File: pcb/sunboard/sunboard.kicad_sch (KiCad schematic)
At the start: 3 parts, among them U1 CD74HC4067M, U2 CD74HC4067M, U3 ESP32-DEVKIT-V1

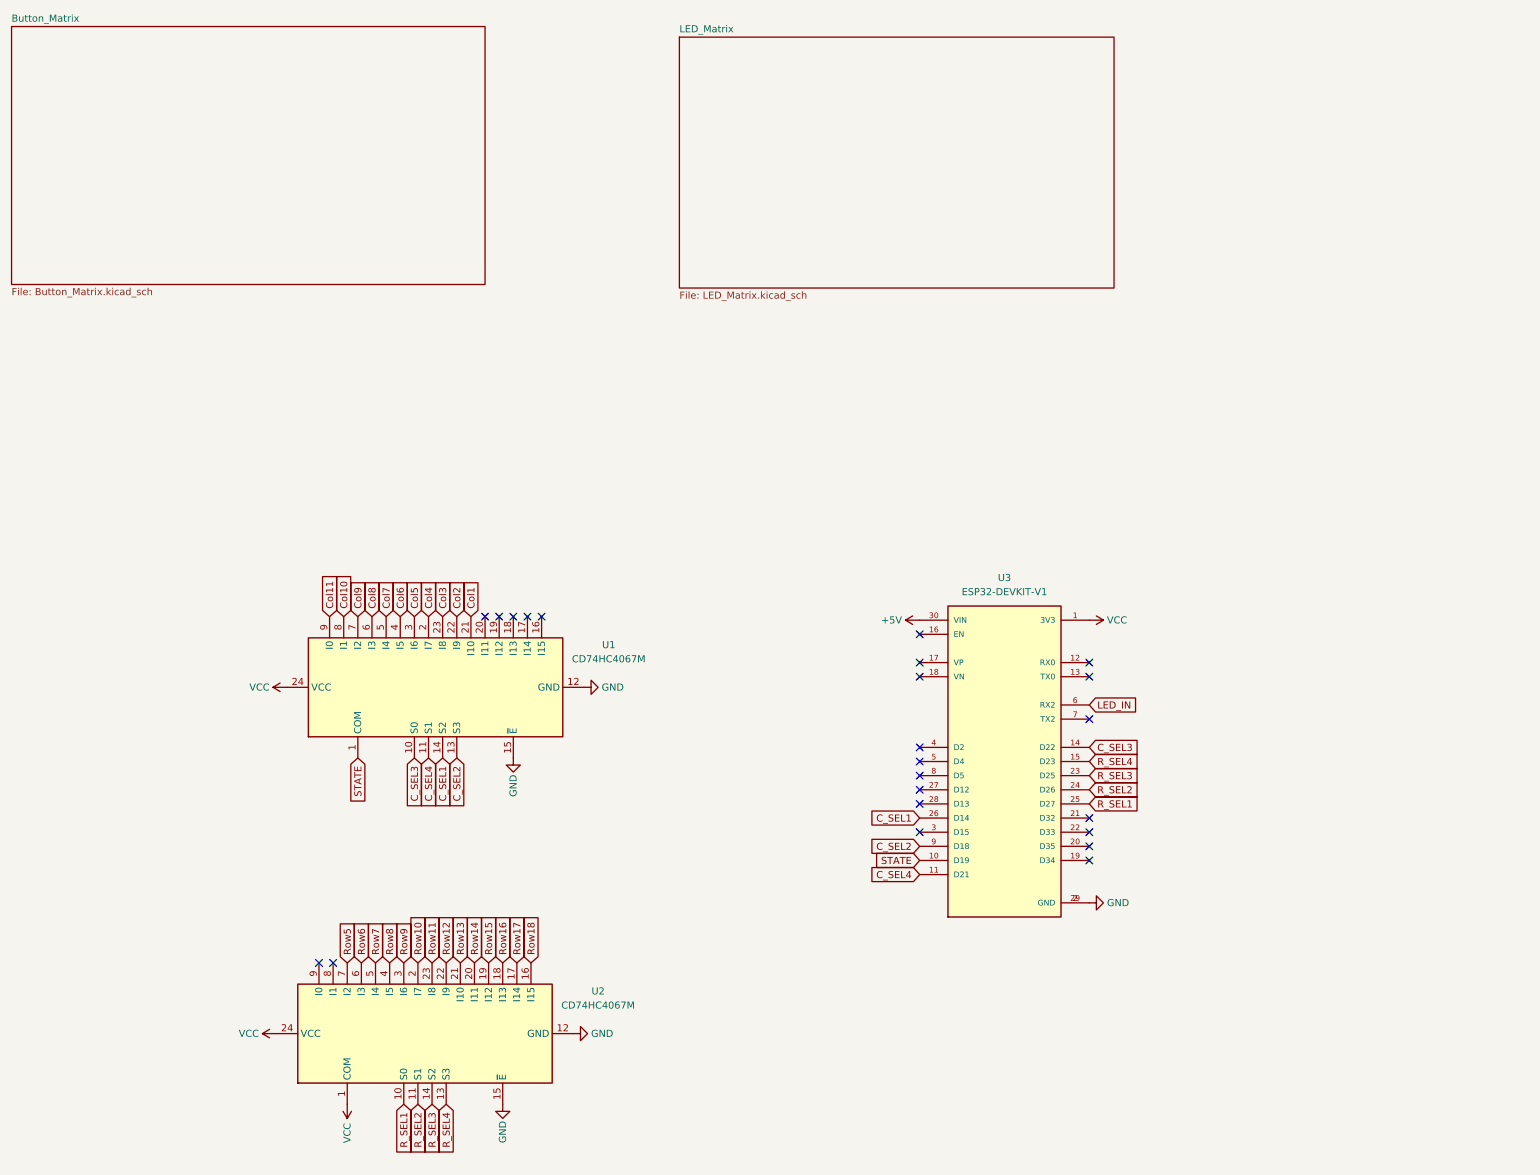
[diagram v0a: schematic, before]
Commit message: feat(pcb): add display
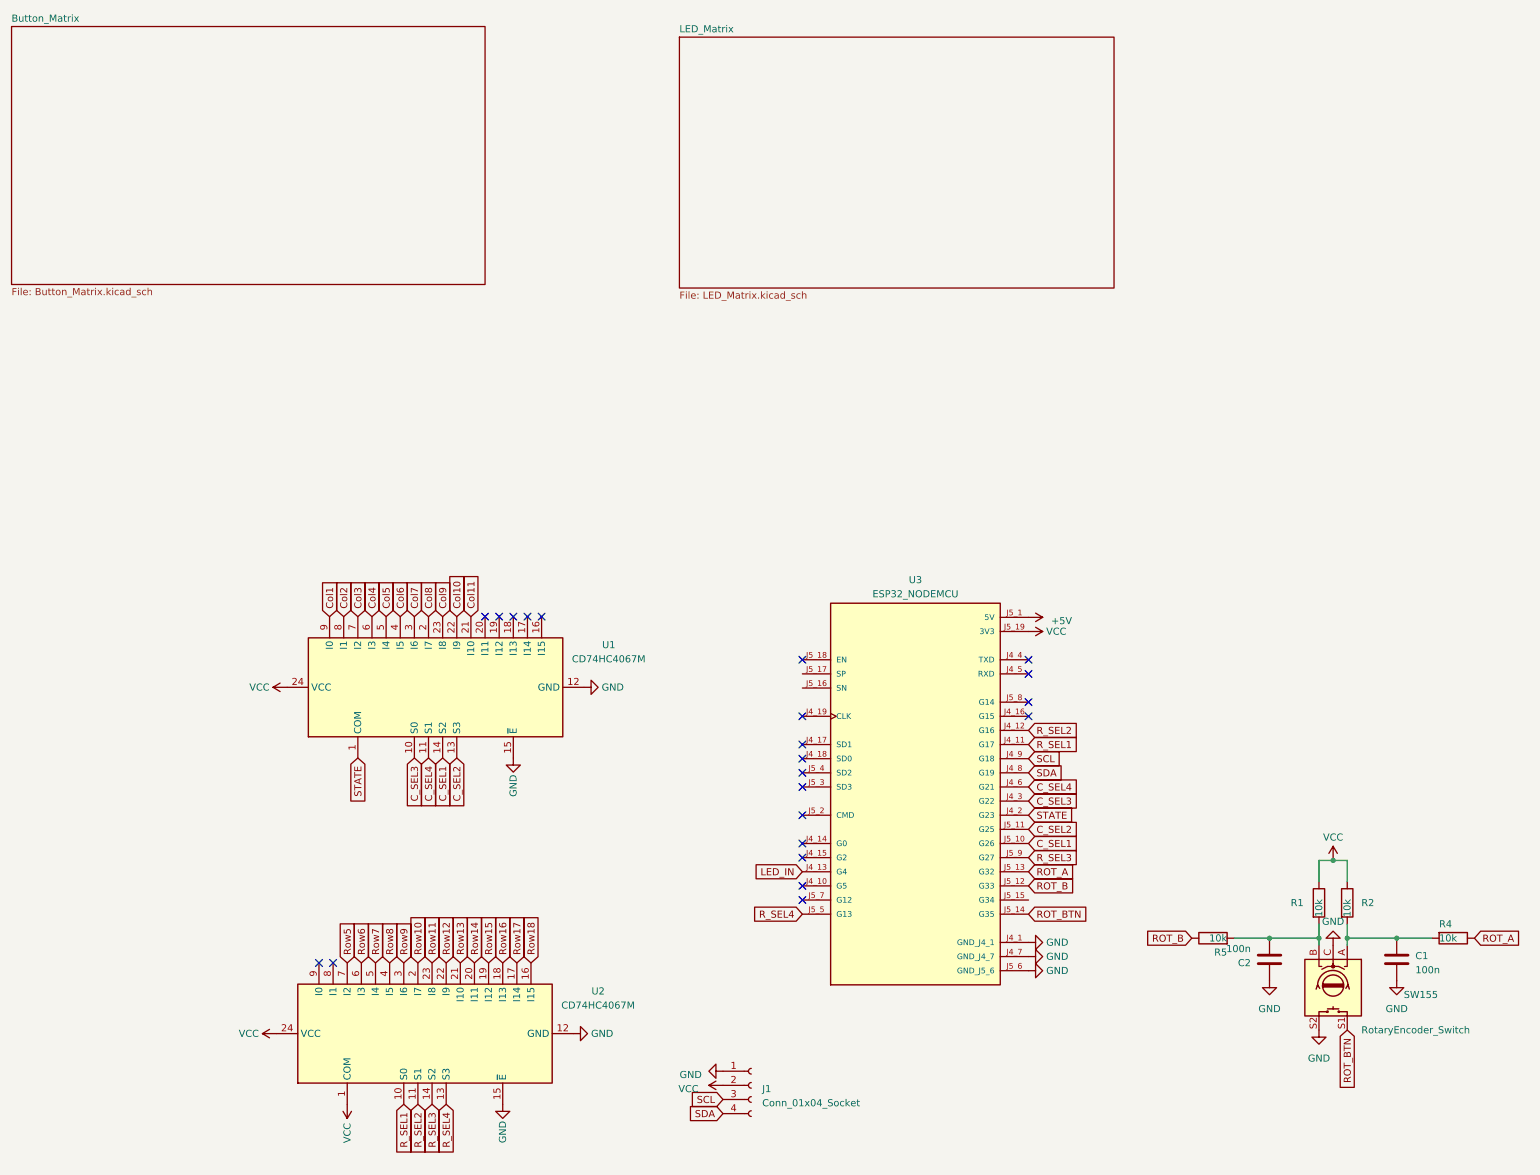
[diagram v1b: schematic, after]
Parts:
- removed U3: ESP32-DEVKIT-V1, ESP32-DEVKIT-V1:MODULE_ESP32_DEVKIT_V1, symbol ESP32-DEVKIT-V1:ESP32-DEVKIT-V1
- added C1, C2: 100n, Capacitor_SMD:C_0805_2012Metric, symbol Device:C
- added J1: Conn_01x04_Socket, Connector_PinSocket_2.54mm:PinSocket_1x04_P2.54mm_Vertical, symbol Connector:Conn_01x04_Socket
- added R1, R2, R4, R5: 10k, Resistor_SMD:R_0805_2012Metric, symbol Device:R
- added SW155: RotaryEncoder_Switch, Rotary_Encoder:RotaryEncoder_Alps_EC12E-Switch_Vertical_H20mm, symbol Device:RotaryEncoder_Switch
- added U3: ESP32_NODEMCU, ESP32_NODEMCU:MODULE_ESP32_NODEMCU, symbol ESP32_NODEMCU:ESP32_NODEMCU
- U1, U2: JLCPCB Part # (none) -> C496123
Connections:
- net +5V: now also U3.J5_1 (5V)
- net C_SEL1: now also U3.J5_10 (G26)
- net C_SEL2: now also U3.J5_11 (G25)
- net C_SEL3: now also U3.J4_3 (G22)
- net C_SEL4: now also U3.J4_6 (G21)
- net Col1: now also U1.9 (I0); no longer U1.21 (I10)
- net Col10: now also U1.22 (I9); no longer U1.8 (I1)
- net Col11: now also U1.21 (I10); no longer U1.9 (I0)
- net Col2: now also U1.8 (I1); no longer U1.22 (I9)
- net Col3: now also U1.7 (I2); no longer U1.23 (I8)
- net Col4: now also U1.6 (I3); no longer U1.2 (I7)
- net Col5: now also U1.5 (I4); no longer U1.3 (I6)
- net Col7: now also U1.3 (I6); no longer U1.5 (I4)
- net Col8: now also U1.2 (I7); no longer U1.6 (I3)
- net Col9: now also U1.23 (I8); no longer U1.7 (I2)
- net GND: now also C1.2, C2.1, J1.1 (Pin_1), SW155.C, SW155.S2, U3.J4_1 (GND_J4_1), U3.J4_7 (GND_J4_7), U3.J5_6 (GND_J5_6)
- net LED_IN: now also U3.J4_13 (G4)
- net R_SEL1: now also U3.J4_11 (G17)
- net R_SEL2: now also U3.J4_12 (G16)
- net R_SEL3: now also U3.J5_9 (G27)
- net R_SEL4: now also U3.J5_5 (G13)
- net STATE: now also U3.J4_2 (G23)
- net VCC: now also J1.2 (Pin_2), R1.1, R2.1, U3.J5_19 (3V3)
- new net: C1.1, R2.2, R4.2, SW155.A
- new net: C2.2, R1.2, R5.2, SW155.B
- new net ROT_A: R4.1, U3.J5_13 (G32)
- new net ROT_B: R5.1, U3.J5_12 (G33)
- new net ROT_BTN: SW155.S1, U3.J5_14 (G35)
- new net SCL: J1.3 (Pin_3), U3.J4_9 (G18)
- new net SDA: J1.4 (Pin_4), U3.J4_8 (G19)
- no-connect marks 23 -> 22

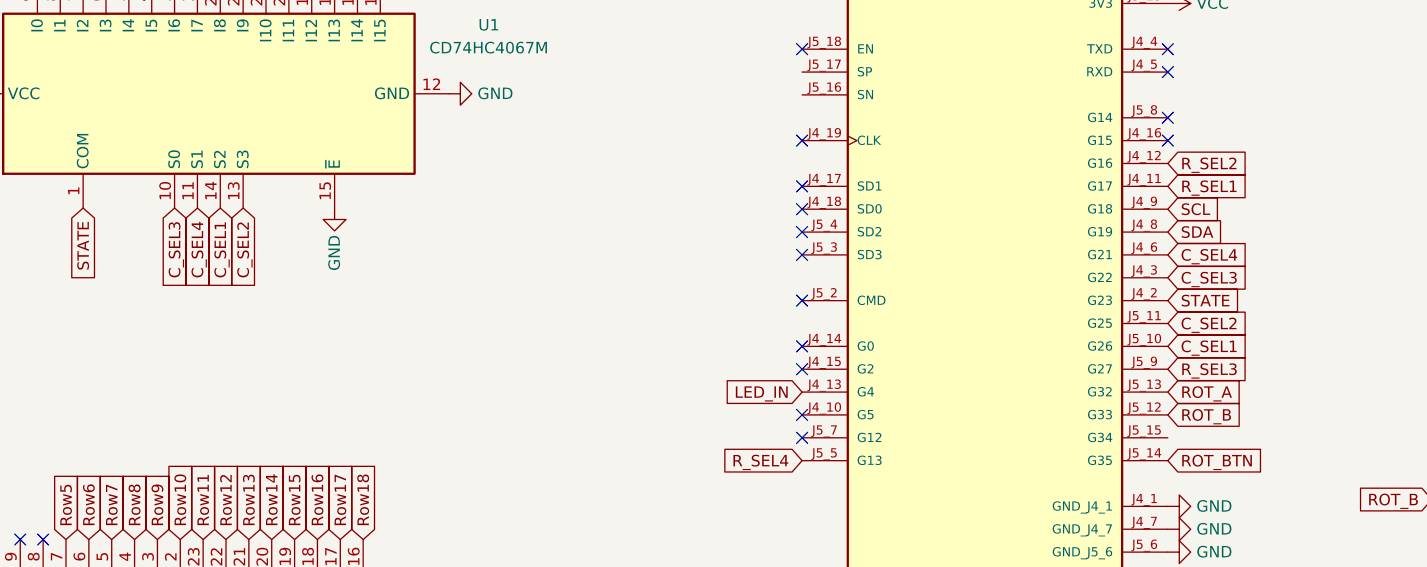
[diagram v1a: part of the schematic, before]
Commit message: feat(pcb): rename some labels
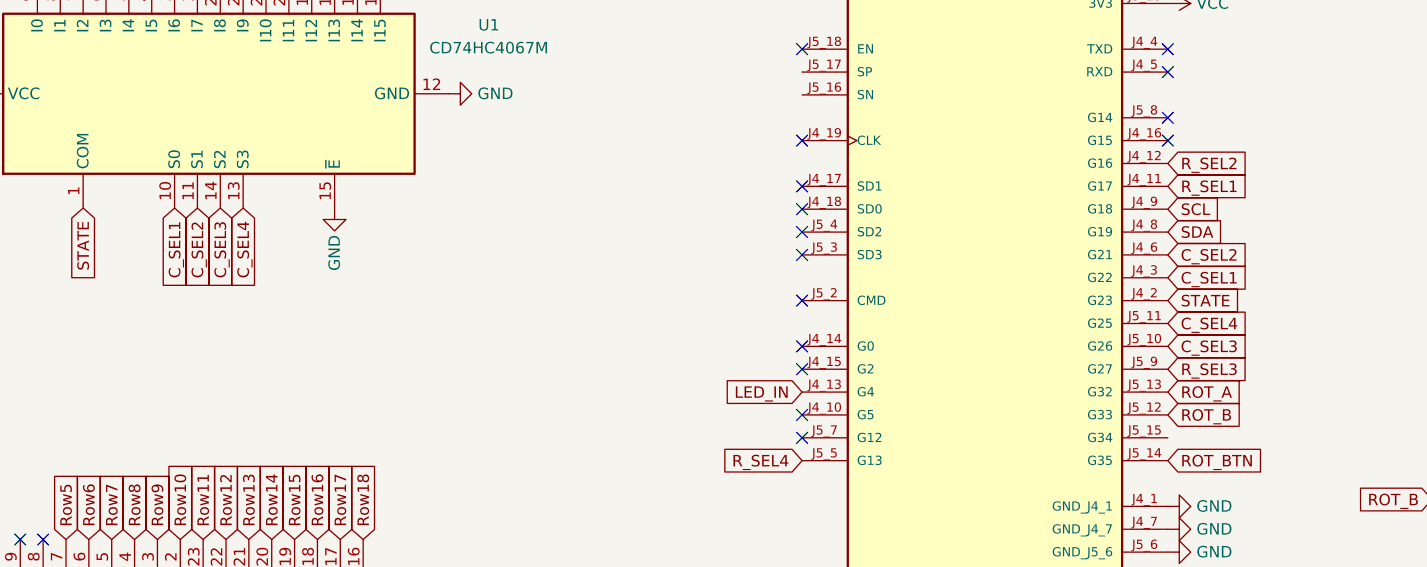
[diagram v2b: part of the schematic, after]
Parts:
- C1, C2: JLCPCB Part # (none) -> C28233
- R1, R2, R4, R5: JLCPCB Part # (none) -> C17414
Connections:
- net C_SEL1: now also U1.10 (S0), U3.J4_3 (G22); no longer U1.14 (S2), U3.J5_10 (G26)
- net C_SEL2: now also U1.11 (S1), U3.J4_6 (G21); no longer U1.13 (S3), U3.J5_11 (G25)
- net C_SEL3: now also U1.14 (S2), U3.J5_10 (G26); no longer U1.10 (S0), U3.J4_3 (G22)
- net C_SEL4: now also U1.13 (S3), U3.J5_11 (G25); no longer U1.11 (S1), U3.J4_6 (G21)
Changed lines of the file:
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@@
     )
   )
-  (global_label "C_SEL2" (shape input) (at 180.213 88.392 0) (fields_autoplaced)
+  (global_label "C_SEL4" (shape input) (at 180.213 88.392 0) (fields_autoplaced)
     (effects (font (size 1.27 1.27)) (justify left))
     (property "Intersheetrefs" "${INTERSHEET_REFS}" (at 189.9525 88.392 0)
@@
     )
   )
-  (global_label "C_SEL1" (shape input) (at 74.93 75.565 270) (fields_autoplaced)
-    (effects (font (size 1.27 1.27)) (justify right))
-    (property "Intersheetrefs" "${INTERSHEET_REFS}" (at 74.8506 84.8119 90)
+  (global_label "C_SEL3" (shape input) (at 74.93 75.565 270) (fields_autoplaced)
+    (effects (font (size 1.27 1.27)) (justify right))
+    (property "Intersheetrefs" "${INTERSHEET_REFS}" (at 74.93 85.3045 90)
       (effects (font (size 1.27 1.27)) (justify right) hide)
     )
@@
     )
   )
-  (global_label "C_SEL3" (shape input) (at 69.85 75.565 270) (fields_autoplaced)
-    (effects (font (size 1.27 1.27)) (justify right))
-    (property "Intersheetrefs" "${INTERSHEET_REFS}" (at 69.7706 84.8119 90)
+  (global_label "C_SEL1" (shape input) (at 69.85 75.565 270) (fields_autoplaced)
+    (effects (font (size 1.27 1.27)) (justify right))
+    (property "Intersheetrefs" "${INTERSHEET_REFS}" (at 69.85 85.3045 90)
       (effects (font (size 1.27 1.27)) (justify right) hide)
     )
@@
     )
   )
-  (global_label "C_SEL1" (shape input) (at 180.213 90.932 0) (fields_autoplaced)
+  (global_label "C_SEL3" (shape input) (at 180.213 90.932 0) (fields_autoplaced)
     (effects (font (size 1.27 1.27)) (justify left))
     (property "Intersheetrefs" "${INTERSHEET_REFS}" (at 189.9525 90.932 0)
@@
     )
   )
-  (global_label "C_SEL2" (shape input) (at 77.47 75.565 270) (fields_autoplaced)
-    (effects (font (size 1.27 1.27)) (justify right))
-    (property "Intersheetrefs" "${INTERSHEET_REFS}" (at 77.3906 84.8119 90)
+  (global_label "C_SEL4" (shape input) (at 77.47 75.565 270) (fields_autoplaced)
+    (effects (font (size 1.27 1.27)) (justify right))
+    (property "Intersheetrefs" "${INTERSHEET_REFS}" (at 77.47 85.3045 90)
       (effects (font (size 1.27 1.27)) (justify right) hide)
     )
@@
     )
   )
-  (global_label "C_SEL4" (shape input) (at 72.39 75.565 270) (fields_autoplaced)
-    (effects (font (size 1.27 1.27)) (justify right))
-    (property "Intersheetrefs" "${INTERSHEET_REFS}" (at 72.3106 84.8119 90)
+  (global_label "C_SEL2" (shape input) (at 72.39 75.565 270) (fields_autoplaced)
+    (effects (font (size 1.27 1.27)) (justify right))
+    (property "Intersheetrefs" "${INTERSHEET_REFS}" (at 72.39 85.3045 90)
       (effects (font (size 1.27 1.27)) (justify right) hide)
     )
@@
     )
   )
-  (global_label "C_SEL3" (shape input) (at 180.213 83.312 0) (fields_autoplaced)
+  (global_label "C_SEL1" (shape input) (at 180.213 83.312 0) (fields_autoplaced)
     (effects (font (size 1.27 1.27)) (justify left))
     (property "Intersheetrefs" "${INTERSHEET_REFS}" (at 189.9525 83.312 0)
@@
     )
   )
-  (global_label "C_SEL4" (shape input) (at 180.213 80.772 0) (fields_autoplaced)
+  (global_label "C_SEL2" (shape input) (at 180.213 80.772 0) (fields_autoplaced)
     (effects (font (size 1.27 1.27)) (justify left))
     (property "Intersheetrefs" "${INTERSHEET_REFS}" (at 189.9525 80.772 0)
@@
       (effects (font (size 1.27 1.27)) hide)
     )
+    (property "JLCPCB Part #" "C28233" (at 246.38 111.76 0)
+      (effects (font (size 1.27 1.27)) hide)
+    )
     (pin "1")
     (pin "2")
@@
     )
     (property "Datasheet" "~" (at 256.54 107.95 0)
+      (effects (font (size 1.27 1.27)) hide)
+    )
+    (property "JLCPCB Part #" "C17414" (at 256.54 107.95 0)
       (effects (font (size 1.27 1.27)) hide)
     )
@@
       (effects (font (size 1.27 1.27)) hide)
     )
+    (property "JLCPCB Part #" "C17414" (at 213.36 107.95 0)
+      (effects (font (size 1.27 1.27)) hide)
+    )
     (pin "1")
     (pin "2")
@@
     )
     (property "Datasheet" "~" (at 232.41 101.6 0)
+      (effects (font (size 1.27 1.27)) hide)
+    )
+    (property "JLCPCB Part #" "C17414" (at 232.41 101.6 0)
       (effects (font (size 1.27 1.27)) hide)
     )
@@
       (effects (font (size 1.27 1.27)) hide)
     )
+    (property "JLCPCB Part #" "C17414" (at 237.49 101.6 0)
+      (effects (font (size 1.27 1.27)) hide)
+    )
     (pin "1")
     (pin "2")
@@
       (effects (font (size 1.27 1.27)) hide)
     )
+    (property "JLCPCB Part #" "C28233" (at 223.52 111.76 0)
+      (effects (font (size 1.27 1.27)) hide)
+    )
